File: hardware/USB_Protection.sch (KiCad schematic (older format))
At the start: 9 parts, among them Q1 DMN6140L, U12 TCPP01-M12

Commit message: schematic should be done, pcb is next
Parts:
- removed D?: SMBJ5.0CA-Q, Diode_SMD:D_0603_1608Metric_Pad1.05x0.95mm_HandSolder, symbol Device:D_Zener_Small
- added C301: 10n, Capacitor_SMD:C_0603_1608Metric_Pad1.05x0.95mm_HandSolder, symbol Device:C_Small
- added FB301: 600R@100MHz, Inductor_SMD:L_0603_1608Metric_Pad1.05x0.95mm_HandSolder, symbol Device:Ferrite_Bead_Small
- added U301: USBLC6-2SC6, Package_TO_SOT_SMD:SOT-23-6, symbol Power_Protection:USBLC6-2SC6
- C1: Manufacturer (none) -> KEMET; Order (none) -> https://www.mouser.at/ProductDetail/80-C0603C104M4R
- F301: renamed from F?; footprint (none) -> Fuse:Fuse_1812_4532Metric_Pad1.30x3.40mm_HandSolder
- Q1: Manufacturer (none) -> Diodes Incorporated; Order (none) -> https://www.mouser.at/ProductDetail/Diodes-Incorporated/DMN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
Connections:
- net labels added: D+_IN, D+_OUT, D-OUT, D-_IN
- wire segments 37 -> 39
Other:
- moved on the sheet: F301
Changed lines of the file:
@@
 $Descr A4 11693 8268
 encoding utf-8
-Sheet 3 4
+Sheet 3 7
 Title ""
 Date ""
@@
 	0    1    1    0
 $EndComp
-Text HLabel 1650 2200 0    50   Input ~ 0
+Text HLabel 750  2200 0    50   Input ~ 0
 VBUS
 Text HLabel 4500 3100 0    50   Input ~ 0
@@
 AR Path="/60604F0C/6060934C/605BE08D" Ref="#PWR?"  Part="1"
 F 0 "#PWR0130" H 5550 3400 50  0001 C CNN
-F 1 "GND" H 5555 3477 50  0000 C CNN
+F 1 "GND" H 5555 3477 50  0001 C CNN
 F 2 "" H 5550 3650 50  0001 C CNN
 F 3 "" H 5550 3650 50  0001 C CNN
@@
 AR Path="/60604F0C/6060934C/605BEA49" Ref="#PWR?"  Part="1"
 F 0 "#PWR0131" H 4450 3400 50  0001 C CNN
-F 1 "GND" H 4455 3477 50  0000 C CNN
+F 1 "GND" H 4455 3477 50  0001 C CNN
 F 2 "" H 4450 3650 50  0001 C CNN
 F 3 "" H 4450 3650 50  0001 C CNN
@@
 F 1 "100n" H 3742 2805 50  0000 L CNN
 F 2 "Capacitor_SMD:C_0603_1608Metric_Pad1.05x0.95mm_HandSolder" H 3650 2850 50  0001 C CNN
-F 3 "~" H 3650 2850 50  0001 C CNN
+F 3 "https://www.mouser.at/datasheet/2/212/KEM_C1002_X7R_SMD-1102033.pdf" H 3650 2850 50  0001 C CNN
+F 4 "KEMET" H 3650 2850 50  0001 C CNN "Manufacturer"
+F 5 "https://www.mouser.at/ProductDetail/80-C0603C104M4R" H 3650 2850 50  0001 C CNN "Order"
 	1    3650 2850
 	1    0    0    -1
@@
 AR Path="/60604F0C/6060934C/605BDB68" Ref="#PWR?"  Part="1"
 F 0 "#PWR0132" H 2100 2250 50  0001 C CNN
-F 1 "GND" H 2105 2327 50  0000 C CNN
+F 1 "GND" H 2105 2327 50  0001 C CNN
 F 2 "" H 2100 2500 50  0001 C CNN
 F 3 "" H 2100 2500 50  0001 C CNN
@@
 AR Path="/60604F0C/6060934C/605C1A8E" Ref="#PWR?"  Part="1"
 F 0 "#PWR0133" H 3000 2550 50  0001 C CNN
-F 1 "GND" H 3005 2627 50  0000 C CNN
+F 1 "GND" H 3005 2627 50  0001 C CNN
 F 2 "" H 3000 2800 50  0001 C CNN
 F 3 "" H 3000 2800 50  0001 C CNN
@@
 AR Path="/60604F0C/6060934C/605CCB83" Ref="#PWR?"  Part="1"
 F 0 "#PWR0136" H 3650 2700 50  0001 C CNN
-F 1 "GND" H 3655 2777 50  0000 C CNN
+F 1 "GND" H 3655 2777 50  0001 C CNN
 F 2 "" H 3650 2950 50  0001 C CNN
 F 3 "" H 3650 2950 50  0001 C CNN
@@
 F 2 "Package_TO_SOT_SMD:SOT-23" H 5200 2225 50  0001 L CIN
 F 3 "http://www.diodes.com/assets/Datasheets/DMN6140L.pdf" H 5000 2300 50  0001 L CNN
+F 4 "Diodes Incorporated" H 5000 2300 50  0001 C CNN "Manufacturer"
+F 5 "https://www.mouser.at/ProductDetail/Diodes-Incorporated/DMN6140L-13?qs=M%2FOdCRO8QQ13uYA06Fe%2F0A%3D%3D" H 5000 2300 50  0001 C CNN "Order"
 	1    5000 2300
 	0    -1   -1   0
 $EndComp
-Wire Wire Line
-	5200 2200 5600 2200
-Wire Wire Line
-	5600 2200 5600 2750
-Wire Wire Line
-	5600 2750 5500 2750
-Text HLabel 5900 2750 2    50   Output ~ 0
+Text HLabel 7350 2750 2    50   Output ~ 0
 5V@500mA
-Connection ~ 5600 2750
 Wire Wire Line
 	3650 2750 4500 2750
 Wire Wire Line
 	3000 2200 3650 2200
-Wire Wire Line
-	5600 2750 5850 2750
-Wire Wire Line
-	5550 3600 5850 3600
 Wire Wire Line
 	5550 3500 5550 3200
@@
 Wire Wire Line
 	5550 3200 5550 3100
-$Comp
-L Device:D_Zener_Small D?
-U 1 1 605F2ABA
-P 5850 3100
-AR Path="/605F2ABA" Ref="D?"  Part="1"
-AR Path="/6071FFAF/605F2ABA" Ref="D?"  Part="1"
-AR Path="/60604F0C/6060934C/605F2ABA" Ref="D?"  Part="1"
-F 0 "D?" V 5804 3170 50  0000 L CNN
-F 1 "SMBJ5.0CA-Q" V 5895 3170 50  0000 L CNN
-F 2 "Diode_SMD:D_0603_1608Metric_Pad1.05x0.95mm_HandSolder" V 5850 3100 50  0001 C CNN
-F 3 "~" V 5850 3100 50  0001 C CNN
-	1    5850 3100
-	0    1    1    0
-$EndComp
-Wire Wire Line
-	5850 2750 5850 3000
-Wire Wire Line
-	5850 3200 5850 3600
 Text Notes 4500 3950 0    50   ~ 0
 Don't need Rd, handled inside the chip
 $Comp
-L Device:Polyfuse_Small F?
+L Device:Polyfuse_Small F301
 U 1 1 6064BF52
-P 1850 2200
-F 0 "F?" V 2055 2200 50  0000 C CNN
-F 1 "1812L050/60MR" V 1964 2200 50  0000 C CNN
-F 2 "" H 1900 2000 50  0001 L CNN
-F 3 "~" H 1850 2200 50  0001 C CNN
-	1    1850 2200
+P 950 2200
+F 0 "F301" V 1155 2200 50  0000 C CNN
+F 1 "1812L050/60MR" V 1064 2200 50  0000 C CNN
+F 2 "Fuse:Fuse_1812_4532Metric_Pad1.30x3.40mm_HandSolder" H 1000 2000 50  0001 L CNN
+F 3 "~" H 950 2200 50  0001 C CNN
+	1    950  2200
 	0    -1   -1   0
 $EndComp
-Wire Wire Line
-	1950 2200 2100 2200
-Wire Wire Line
-	1850 2200 1750 2200
 Wire Wire Line
 	3650 2400 3650 2200
@@
 	3650 2600 3650 2750
 Connection ~ 3650 2750
-Connection ~ 1750 2200
-Wire Wire Line
-	1750 2200 1650 2200
+Wire Wire Line
+	850  2200 750  2200
 Wire Wire Line
 	3000 2200 3000 2300
@@
 	3000 2200 2100 2200
 Connection ~ 3000 2200
+Connection ~ 5850 2750
+Wire Wire Line
+	5500 2750 5850 2750
+Wire Wire Line
+	5850 2750 5850 2200
+Wire Wire Line
+	5200 2200 5850 2200
+$Comp
+L Power_Protection:USBLC6-2SC6 U301
+U 1 1 605F9EDA
+P 6650 3200
+F 0 "U301" H 6400 3550 50  0000 C CNN
+F 1 "USBLC6-2SC6" H 7000 3550 50  0000 C CNN
+F 2 "Package_TO_SOT_SMD:SOT-23-6" H 6650 2700 50  0001 C CNN
+F 3 "https://www.st.com/resource/en/datasheet/usblc6-2.pdf" H 6850 3550 50  0001 C CNN
+	1    6650 3200
+	1    0    0    -1
+$EndComp
+Wire Wire Line
+	7350 2750 6650 2750
+Wire Wire Line
+	6650 2750 6650 2800
+Wire Wire Line
+	5850 2750 6650 2750
+Connection ~ 6650 2750
+Wire Wire Line
+	5550 3600 6650 3600
+Text HLabel 7050 3300 2    50   Input ~ 0
+D+_IN
+Text HLabel 6250 3300 0    50   Input ~ 0
+D-_IN
+Text HLabel 7050 3100 2    50   Output ~ 0
+D+_OUT
+Text HLabel 6250 3100 0    50   Output ~ 0
+D-OUT
+$Comp
+L Device:Ferrite_Bead_Small FB301
+U 1 1 60600B0B
+P 1850 2200
+F 0 "FB301" V 1613 2200 50  0000 C CNN
+F 1 "600R@100MHz" V 1704 2200 50  0000 C CNN
+F 2 "Inductor_SMD:L_0603_1608Metric_Pad1.05x0.95mm_HandSolder" V 1780 2200 50  0001 C CNN
+F 3 "MI0603J601R-10" H 1850 2200 50  0001 C CNN
+	1    1850 2200
+	0    1    1    0
+$EndComp
+Wire Wire Line
+	1950 2200 2100 2200
 Connection ~ 2100 2200
 Wire Wire Line
-	5900 2750 5850 2750
-Connection ~ 5850 2750
+	1750 2200 1350 2200
+$Comp
+L Device:C_Small C301
+U 1 1 60602FFA
+P 1350 2350
+AR Path="/6071FFAF/60602FFA" Ref="C301"  Part="1"
+AR Path="/60604F0C/6060934C/60602FFA" Ref="C?"  Part="1"
+F 0 "C301" H 1442 2396 50  0000 L CNN
+F 1 "10n" H 1442 2305 50  0000 L CNN
+F 2 "Capacitor_SMD:C_0603_1608Metric_Pad1.05x0.95mm_HandSolder" H 1350 2350 50  0001 C CNN
+F 3 "~" H 1350 2350 50  0001 C CNN
+	1    1350 2350
+	1    0    0    -1
+$EndComp
+Wire Wire Line
+	1350 2250 1350 2200
+Connection ~ 1350 2200
+Wire Wire Line
+	1350 2200 1050 2200
+$Comp
+L power:GND #PWR0122
+U 1 1 60603C38
+P 1350 2500
+AR Path="/6071FFAF/60603C38" Ref="#PWR0122"  Part="1"
+AR Path="/60604F0C/6060934C/60603C38" Ref="#PWR?"  Part="1"
+F 0 "#PWR0122" H 1350 2250 50  0001 C CNN
+F 1 "GND" H 1355 2327 50  0001 C CNN
+F 2 "" H 1350 2500 50  0001 C CNN
+F 3 "" H 1350 2500 50  0001 C CNN
+	1    1350 2500
+	1    0    0    -1
+$EndComp
+Wire Wire Line
+	1350 2500 1350 2450
 $EndSCHEMATC

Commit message: wip hw
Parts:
- C1, C301: footprint Capacitor_SMD:C_0603_1608Metric_Pad1.05x0.95mm_HandSolder -> Capacitor_SMD:C_0603_1608Metric
- D1, D2: footprint Diode_SMD:D_0603_1608Metric_Pad1.05x0.95mm_HandSolder -> Diode_SMD:D_0603_1608Metric
- F301: footprint Fuse:Fuse_1812_4532Metric_Pad1.30x3.40mm_HandSolder -> Fuse:Fuse_1812_4532Metric
- FB301: footprint Inductor_SMD:L_0603_1608Metric_Pad1.05x0.95mm_HandSolder -> Inductor_SMD:L_0603_1608Metric
- R10, R11: footprint Resistor_SMD:R_0603_1608Metric_Pad1.05x0.95mm_HandSolder -> Resistor_SMD:R_0603_1608Metric
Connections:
- net D+_IN renamed IN_D+
- net D+_OUT renamed OUT_D+
- net D-OUT renamed OUT_D-
- net D-_IN renamed IN_D-
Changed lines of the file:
@@
 F 0 "D1" V 2054 2470 50  0000 L CNN
 F 1 "ESDA25P35-1U1M" V 2145 2470 50  0000 L CNN
-F 2 "Diode_SMD:D_0603_1608Metric_Pad1.05x0.95mm_HandSolder" V 2100 2400 50  0001 C CNN
+F 2 "Diode_SMD:D_0603_1608Metric" V 2100 2400 50  0001 C CNN
 F 3 "~" V 2100 2400 50  0001 C CNN
 	1    2100 2400
@@
 F 0 "R10" H 3059 2446 50  0000 L CNN
 F 1 "10k" H 3059 2355 50  0000 L CNN
-F 2 "Resistor_SMD:R_0603_1608Metric_Pad1.05x0.95mm_HandSolder" H 3000 2400 50  0001 C CNN
+F 2 "Resistor_SMD:R_0603_1608Metric" H 3000 2400 50  0001 C CNN
 F 3 "~" H 3000 2400 50  0001 C CNN
 	1    3000 2400
@@
 F 0 "R11" H 3059 2746 50  0000 L CNN
 F 1 "2k7" H 3059 2655 50  0000 L CNN
-F 2 "Resistor_SMD:R_0603_1608Metric_Pad1.05x0.95mm_HandSolder" H 3000 2700 50  0001 C CNN
+F 2 "Resistor_SMD:R_0603_1608Metric" H 3000 2700 50  0001 C CNN
 F 3 "~" H 3000 2700 50  0001 C CNN
 	1    3000 2700
@@
 F 0 "D2" V 3750 2400 50  0000 C CNN
 F 1 "NSR20F30NXT5G" V 3550 2150 50  0000 C CNN
-F 2 "Diode_SMD:D_0603_1608Metric_Pad1.05x0.95mm_HandSolder" V 3650 2500 50  0001 C CNN
+F 2 "Diode_SMD:D_0603_1608Metric" V 3650 2500 50  0001 C CNN
 F 3 "~" V 3650 2500 50  0001 C CNN
 	1    3650 2500
@@
 F 0 "C1" H 3742 2896 50  0000 L CNN
 F 1 "100n" H 3742 2805 50  0000 L CNN
-F 2 "Capacitor_SMD:C_0603_1608Metric_Pad1.05x0.95mm_HandSolder" H 3650 2850 50  0001 C CNN
+F 2 "Capacitor_SMD:C_0603_1608Metric" H 3650 2850 50  0001 C CNN
 F 3 "https://www.mouser.at/datasheet/2/212/KEM_C1002_X7R_SMD-1102033.pdf" H 3650 2850 50  0001 C CNN
 F 4 "KEMET" H 3650 2850 50  0001 C CNN "Manufacturer"
@@
 F 0 "F301" V 1155 2200 50  0000 C CNN
 F 1 "1812L050/60MR" V 1064 2200 50  0000 C CNN
-F 2 "Fuse:Fuse_1812_4532Metric_Pad1.30x3.40mm_HandSolder" H 1000 2000 50  0001 L CNN
+F 2 "Fuse:Fuse_1812_4532Metric" H 1000 2000 50  0001 L CNN
 F 3 "~" H 950 2200 50  0001 C CNN
 	1    950  2200
@@
 Wire Wire Line
 	5550 3600 6650 3600
-Text HLabel 7050 3300 2    50   Input ~ 0
-D+_IN
-Text HLabel 6250 3300 0    50   Input ~ 0
-D-_IN
-Text HLabel 7050 3100 2    50   Output ~ 0
-D+_OUT
-Text HLabel 6250 3100 0    50   Output ~ 0
-D-OUT
 $Comp
 L Device:Ferrite_Bead_Small FB301
@@
 F 0 "FB301" V 1613 2200 50  0000 C CNN
 F 1 "600R@100MHz" V 1704 2200 50  0000 C CNN
-F 2 "Inductor_SMD:L_0603_1608Metric_Pad1.05x0.95mm_HandSolder" V 1780 2200 50  0001 C CNN
+F 2 "Inductor_SMD:L_0603_1608Metric" V 1780 2200 50  0001 C CNN
 F 3 "MI0603J601R-10" H 1850 2200 50  0001 C CNN
 	1    1850 2200
@@
 F 0 "C301" H 1442 2396 50  0000 L CNN
 F 1 "10n" H 1442 2305 50  0000 L CNN
-F 2 "Capacitor_SMD:C_0603_1608Metric_Pad1.05x0.95mm_HandSolder" H 1350 2350 50  0001 C CNN
+F 2 "Capacitor_SMD:C_0603_1608Metric" H 1350 2350 50  0001 C CNN
 F 3 "~" H 1350 2350 50  0001 C CNN
 	1    1350 2350
@@
 Wire Wire Line
 	1350 2500 1350 2450
+Text HLabel 7050 3100 2    50   Output ~ 0
+OUT_D+
+Text HLabel 6250 3100 0    50   Output ~ 0
+OUT_D-
+Text HLabel 7050 3300 2    50   Input ~ 0
+IN_D+
+Text HLabel 6250 3300 0    50   Input ~ 0
+IN_D-
 $EndSCHEMATC

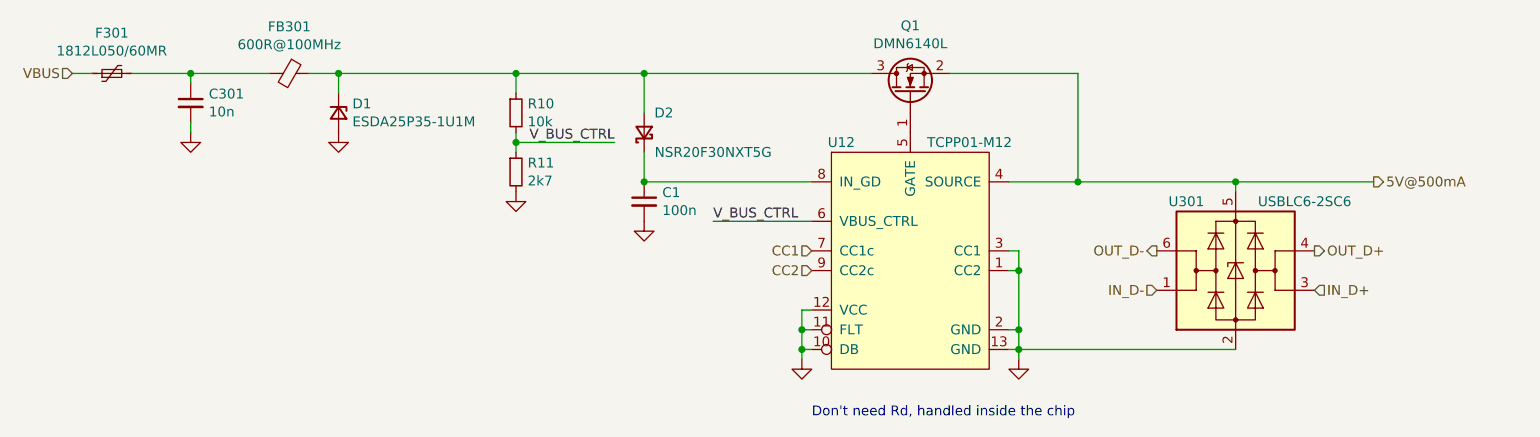
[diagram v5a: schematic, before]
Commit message: added powerflags
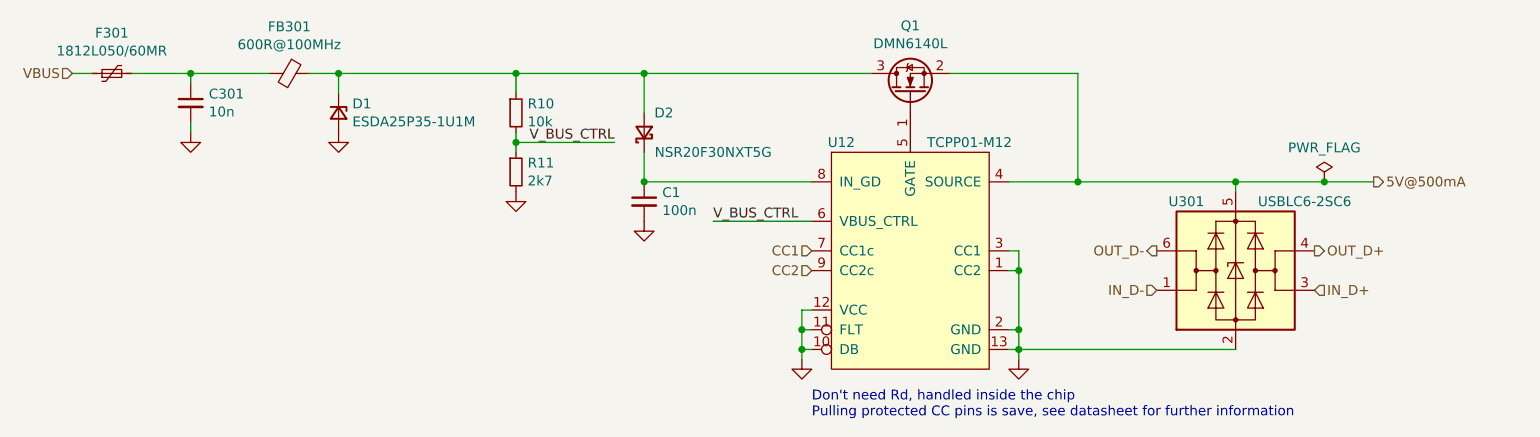
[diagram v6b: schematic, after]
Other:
- note added: "Don't need Rd, handled inside the chip\nPulling protected CC pins is save, see datasheet for further information"
- note removed: "Don't need Rd, handled inside the chip"
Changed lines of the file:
@@
 	5550 3200 5550 3100
 Text Notes 4500 3950 0    50   ~ 0
-Don't need Rd, handled inside the chip
+Don't need Rd, handled inside the chip\nPulling protected CC pins is save, see datasheet for further information
 $Comp
 L Device:Polyfuse_Small F301
@@
 $EndComp
 Wire Wire Line
-	7350 2750 6650 2750
+	7350 2750 7100 2750
 Wire Wire Line
 	6650 2750 6650 2800
@@
 Text HLabel 6250 3300 0    50   Input ~ 0
 IN_D-
+$Comp
+L power:PWR_FLAG #FLG0102
+U 1 1 606A9573
+P 7100 2750
+F 0 "#FLG0102" H 7100 2825 50  0001 C CNN
+F 1 "PWR_FLAG" H 7100 2923 50  0000 C CNN
+F 2 "" H 7100 2750 50  0001 C CNN
+F 3 "~" H 7100 2750 50  0001 C CNN
+	1    7100 2750
+	1    0    0    -1
+$EndComp
+Connection ~ 7100 2750
+Wire Wire Line
+	7100 2750 6650 2750
 $EndSCHEMATC

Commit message: minor improvements
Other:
- note added: "C1: 50V X7R"
- note added: "Don't need Rd, handled inside the chip\nPulling protected CC pins low is save, see datasheet for further information"
- note removed: "Don't need Rd, handled inside the chip\nPulling protected CC pins is save, see datasheet for further information"
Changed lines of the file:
@@
 	5550 3200 5550 3100
 Text Notes 4500 3950 0    50   ~ 0
-Don't need Rd, handled inside the chip\nPulling protected CC pins is save, see datasheet for further information
+Don't need Rd, handled inside the chip\nPulling protected CC pins low is save, see datasheet for further information
 $Comp
 L Device:Polyfuse_Small F301
@@
 Wire Wire Line
 	7100 2750 6650 2750
+Text Notes 3350 3250 0    50   ~ 0
+C1: 50V X7R
 $EndSCHEMATC
